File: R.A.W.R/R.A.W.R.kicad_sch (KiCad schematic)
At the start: 15 parts, among them IC1 PSA4-5043+, J1 BNC connector

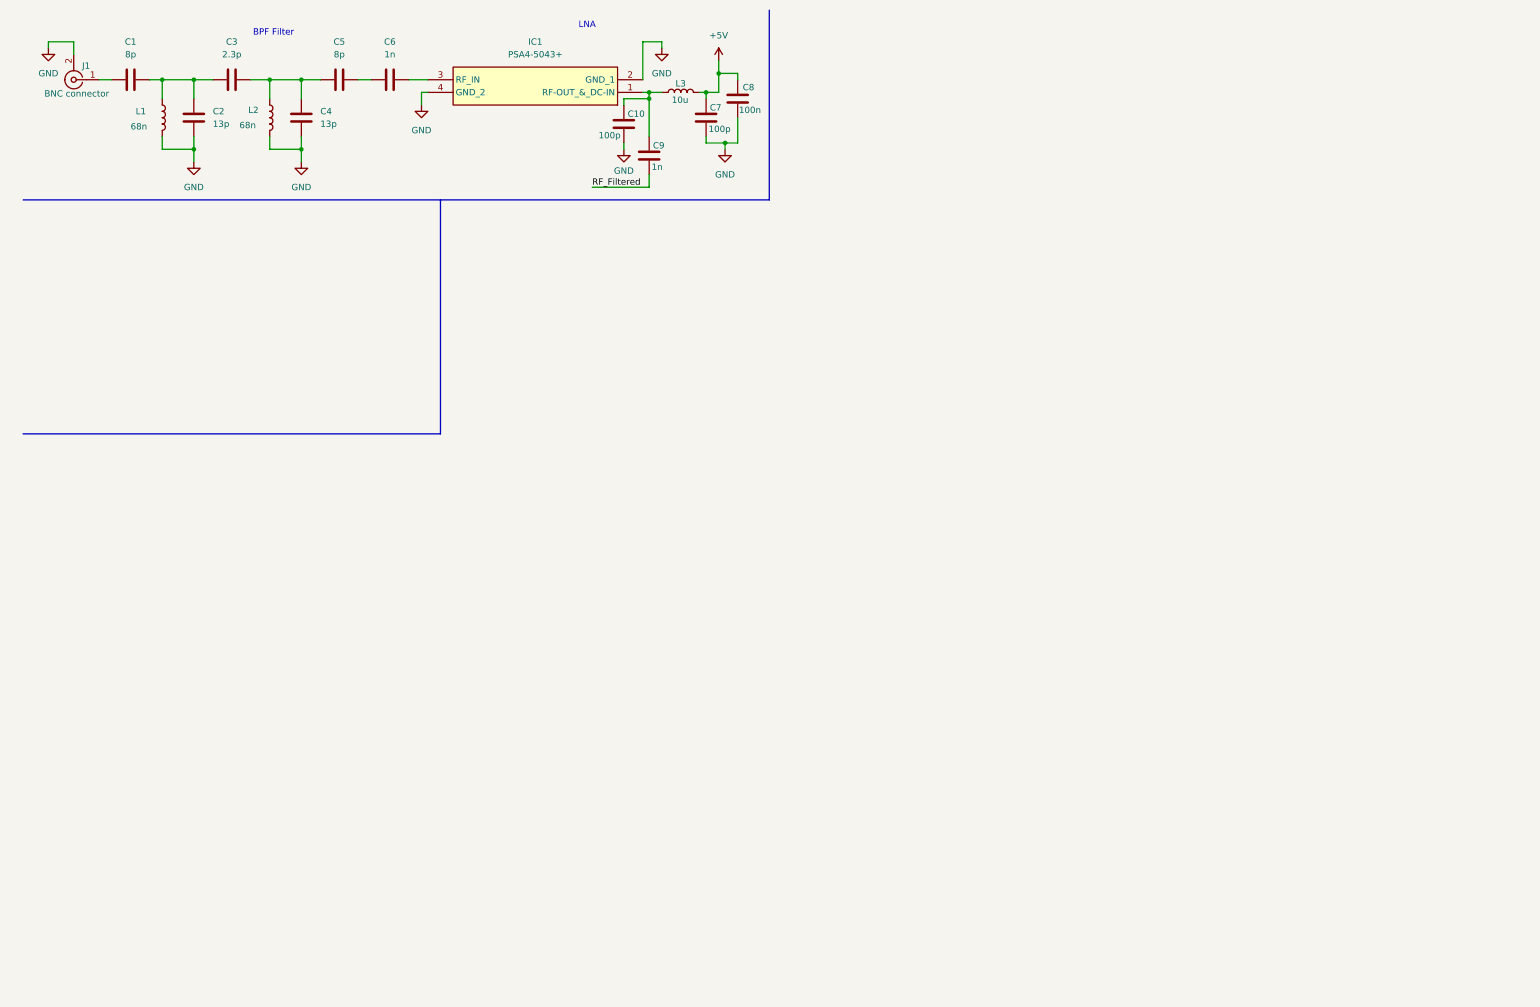
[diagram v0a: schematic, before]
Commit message: Added mixer, 10.7MHz filter, AM demodulator, audio amp and speaker
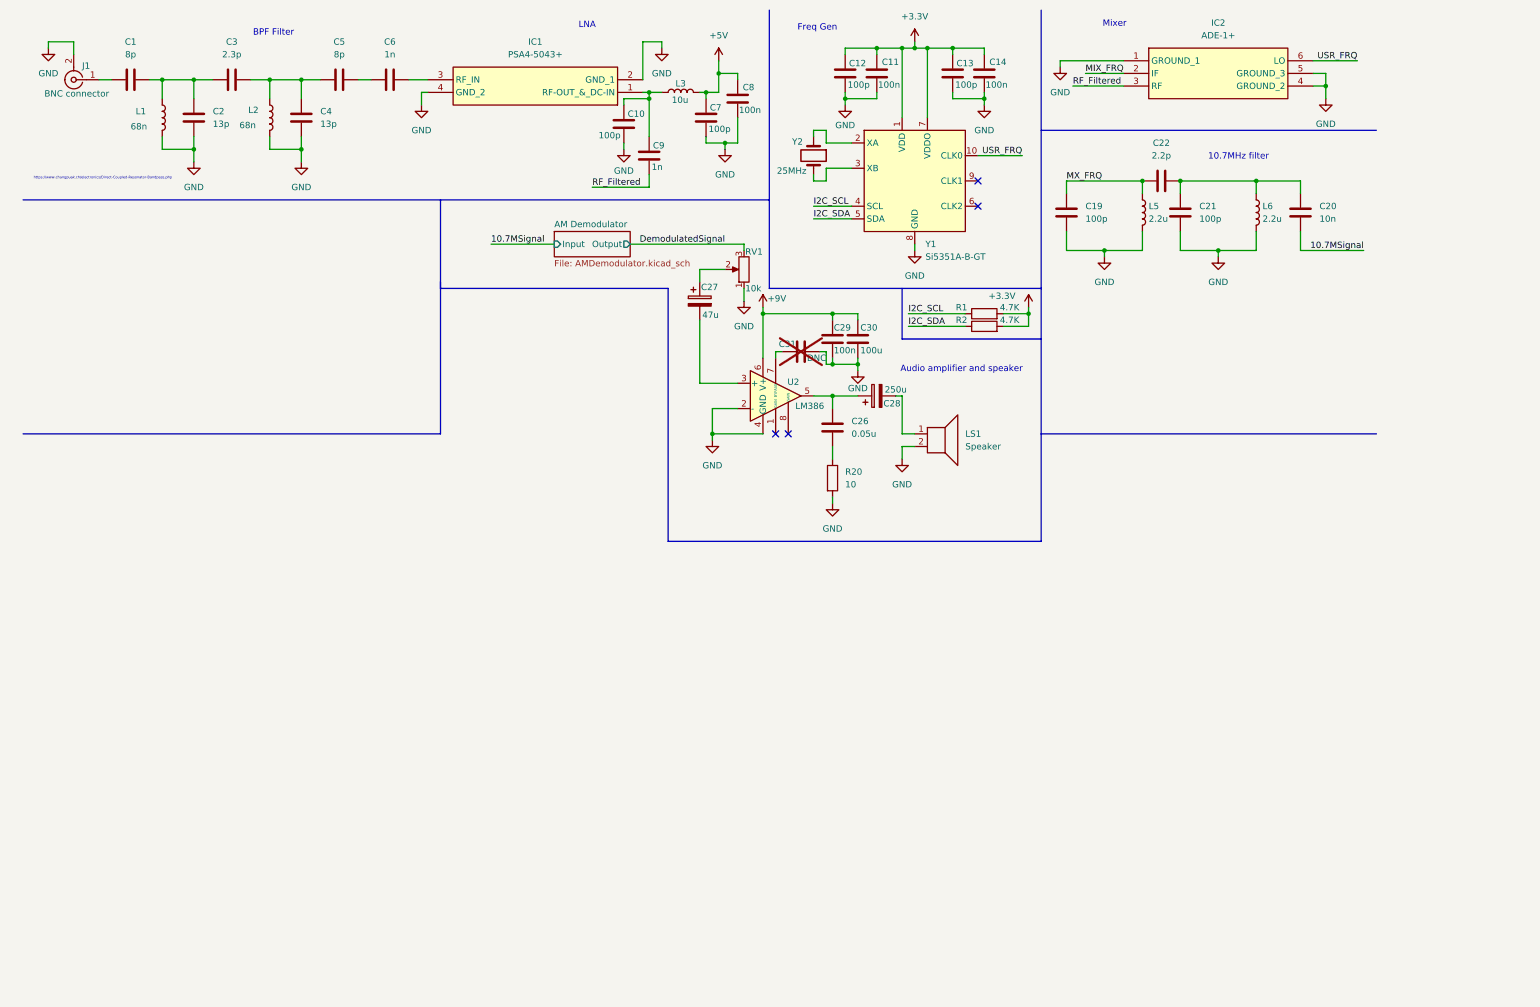
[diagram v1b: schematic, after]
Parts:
- added C11, C14, C29: 100n, symbol Device:C
- added C12, C13, C19, C21: 100p, symbol Device:C
- added C20: 10n, symbol Device:C
- added C22: 2.2p, symbol Device:C
- added C26: 0.05u, symbol Device:C
- added C27: 47u, symbol Device:C_Polarized
- added C28: 250u, symbol Device:C_Polarized
- added C30: 100u, symbol Device:C
- added C31: DNC, symbol Device:C
- added IC2: ADE-1+, ADE1, symbol RAWR:ADE-1+
- added L5, L6: 2.2u, Package_SO:SOIC-20W_7.5x12.8mm_P1.27mm, symbol Device:L
- added LS1: Speaker, Package_SON:WSON-8-1EP_6x5mm_P1.27mm_EP3.4x4mm, symbol Device:Speaker
- added R1, R2: 4.7K, symbol Device:R
- added R20: 10, symbol Device:R
- added RV1: 10k, Package_SO:TSSOP-20_4.4x6.5mm_P0.65mm, symbol Device:R_Potentiometer
- added U2: LM386, Package_DIP:DIP-14_W7.62mm, symbol Amplifier_Audio:LM386
- added Y1: Si5351A-B-GT, Package_SO:MSOP-10_3x3mm_P0.5mm, symbol Oscillator:Si5351A-B-GT
- added Y2: 25MHz, symbol Device:Crystal
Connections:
- net GND: now also C11.1, C12.1, C13.1, C14.1, C19.2, C21.2, C29.2, C30.2, C31.2, IC2.1 (GROUND_1), IC2.4 (GROUND_2), IC2.5 (GROUND_3), L5.2, L6.2, LS1.2, R20.2, RV1.1, U2.2 (-), U2.4 (GND), Y1.8 (GND)
- net RF_Filtered: now also IC2.3 (RF)
- new net: C27.1, RV1.2
- new net: C27.2, U2.3 (+)
- new net: C26.2, R20.1
- new net: C20.1, C21.1, C22.2, L6.1
- new net: C26.1, C28.1, U2.5
- new net: C28.2, LS1.1
- new net: Y1.2 (XA), Y2.1
- new net: Y1.3 (XB), Y2.2
- new net: C31.1, U2.7 (BYPASS)
- new net +3.3V: C11.2, C12.2, C13.2, C14.2, R1.2, R2.2, Y1.1 (VDD), Y1.7 (VDDO)
- new net +9V: C29.1, C30.1, U2.6 (V+)
- new net 10.7MSignal: C20.2
- new net DemodulatedSignal: RV1.3
- new net I2C_SCL: R1.1, Y1.4 (SCL)
- new net I2C_SDA: R2.1, Y1.5 (SDA)
- new net MIX_FRQ: IC2.2 (IF)
- new net MX_FRQ: C19.1, C22.1, L5.1
- new net USR_FRQ: IC2.6 (LO), Y1.10 (CLK0)
- no-connect marks 0 -> 4
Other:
- added sheet AM Demodulator (AMDemodulator.kicad_sch)
- note added: "10.7MHz filter"
- note added: "Audio amplifier and speaker"
- note added: "Freq Gen"
- note added: "Mixer"
- note added: "https://www.changpuak.ch/electronics/Direct-Coupled-Resonator-Bandpass.php"
- company: (none) -> Author: Wiktor Kociuba
- title: (none) -> R.A.W.R.

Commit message: Added RP2354A, screen and rotary encoder
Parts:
- added J3: 0.96 inch screen, Package_DFN_QFN:NXP_LQFN-48-1EP_7x7mm_P0.5mm_EP3.5x3.5mm_16xMask0.45x0.45_ThermalVias, symbol Connector:Conn_01x04_Pin
- added R27, R28, R29, R30, R31: 4.7K, symbol Device:R
- added SW3: RotaryEncoder_Switch, symbol Device:RotaryEncoder_Switch
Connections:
- net +3.3V: now also R27.2, R28.2
- net GND: now also J3.4 (Pin_4), SW3.C, SW3.S2
- new net +3V3: J3.3 (Pin_3), R29.2, R30.2, R31.2
- new net EncoderA: R29.1, SW3.A
- new net EncoderB: R30.1, SW3.B
- new net EncoderSW: R31.1, SW3.S1
- new net I2C1_SCL: J3.2 (Pin_2), R27.1
- new net I2C1_SDA: J3.1 (Pin_1), R28.1
- no-connect marks 4 -> 27
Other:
- added sheet MCU (MCU.kicad_sch)

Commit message: Added some footprints and USB-C receptacle
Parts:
- added C47, C48: 8p-30p, Capacitor_SMD:C_Trimmer_Murata_TZC3, symbol Device:C_Variable
- C1, C10, C11, C12, C13, C14, C2, C20, C22, C26, C29, C3, C31, C4, C5, C6, C7, C8, C9: footprint (none) -> Capacitor_SMD:C_0805_2012Metric_Pad1.18x1.45mm_HandSolder
- C19, C21: value 100p -> 82p; footprint (none) -> Capacitor_SMD:C_0805_2012Metric_Pad1.18x1.45mm_HandSolder
- C27, C28, C30: footprint (none) -> Capacitor_THT:CP_Radial_D8.0mm_P5.00mm
- IC1: footprint PSA45043 -> RAWR:PSA45043
- IC2: footprint ADE1 -> RAWR:ADE1
- J1: footprint Filter:Filter_Murata_BNX025 -> Connector_Coaxial:BNC_Amphenol_031-6575_Horizontal
- J3: footprint Package_DFN_QFN:NXP_LQFN-48-1EP_7x7mm_P0.5mm_EP3.5x3.5mm_16xMask0.45x0.45_ThermalVias -> Connector_PinHeader_2.54mm:PinHeader_1x04_P2.54mm_Vertical
- L1, L2, L3: footprint Package_SO:SOIC-20W_7.5x12.8mm_P1.27mm -> Inductor_SMD:L_0805_2012Metric_Pad1.05x1.20mm_HandSolder
- L5, L6: footprint Package_SO:SOIC-20W_7.5x12.8mm_P1.27mm -> Capacitor_SMD:C_0805_2012Metric_Pad1.18x1.45mm_HandSolder
- LS1: footprint Package_SON:WSON-8-1EP_6x5mm_P1.27mm_EP3.4x4mm -> Connector_PinHeader_2.54mm:PinHeader_1x02_P2.54mm_Vertical
- R1, R2, R20, R27, R28, R29, R30, R31: footprint (none) -> Resistor_SMD:R_0805_2012Metric_Pad1.20x1.40mm_HandSolder
- RV1: footprint Package_SO:TSSOP-20_4.4x6.5mm_P0.65mm -> (none)
- U2: footprint Package_DIP:DIP-14_W7.62mm -> (none)
- Y1: footprint Package_SO:MSOP-10_3x3mm_P0.5mm -> RAWR:SOP50P490X110-10N
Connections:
- net GND: now also C47.2, C48.2
- net MX_FRQ: now also C47.1
- net at C20.1, C21.1, C22.2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: now also C48.1

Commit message: Finished assignment of footprints
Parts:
- RV1: footprint (none) -> RAWR:PTV09A2020FA104
- SW3: footprint (none) -> RAWR:PEC11R4220FS0024
- U2: footprint (none) -> RAWR:SOIC127P600X175-8N
- Y2: footprint (none) -> Crystal:Crystal_SMD_5032-2Pin_5.0x3.2mm_HandSoldering
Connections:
- net MX_FRQ is gone; now on net MIX_FRQ: C19.1, C22.1, C47.1, L5.1
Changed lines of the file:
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@@
 		)
 	)
-	(label "MX_FRQ"
+	(label "MIX_FRQ"
 		(at 222.25 46.99 0)
 		(effects
@@
 			)
 		)
-		(property "Footprint" ""
+		(property "Footprint" "RAWR:PTV09A2020FA104"
 			(at 157.48 64.77 0)
 			(hide yes)
@@
 			)
 		)
-		(property "Footprint" ""
+		(property "Footprint" "Crystal:Crystal_SMD_5032-2Pin_5.0x3.2mm_HandSoldering"
 			(at 171.45 41.91 0)
 			(hide yes)
@@
 			)
 		)
-		(property "Footprint" ""
+		(property "Footprint" "RAWR:SOIC127P600X175-8N"
 			(at 166.37 87.63 0)
 			(hide yes)
@@
 			)
 		)
-		(property "Footprint" ""
+		(property "Footprint" "RAWR:PEC11R4220FS0024"
 			(at 45.72 126.746 0)
 			(hide yes)

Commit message: Added charger, 3v3 regulator and 10v5 stepup
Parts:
- added BT1: 18650 Li-Ion, Package_DFN_QFN:Texas_RGE0024H_VQFN-24-1EP_4x4mm_P0.5mm_EP2.7x2.7mm, symbol Device:Battery_Cell
- added C49, C51: 4.7u, QFN50P300X300X100-17N-D, symbol Device:C
- added C50, C66: 1u, QFN50P300X300X100-17N-D, symbol Device:C
- added C52: 100n, QFN50P300X300X100-17N-D, symbol Device:C
- added C53, C54, C58: 10u, QFN50P300X300X100-17N-D, symbol Device:C
- added C55, C56, C57, C63, C64, C65: 22u, QFN50P300X300X100-17N-D, symbol Device:C
- added C59, C67: 0.1u, QFN50P300X300X100-17N-D, symbol Device:C
- added C60: 2.2u, QFN50P300X300X100-17N-D, symbol Device:C
- added C61: 10n, QFN50P300X300X100-17N-D, symbol Device:C
- added C62: 100p, QFN50P300X300X100-17N-D, symbol Device:C
- added C68: 47n, QFN50P300X300X100-17N-D, symbol Device:C
- added D2: GREEN, symbol Device:LED
- added D3: RED, symbol Device:LED
- added IC3: BQ24075QRGTRQ1, QFN50P300X300X100-17N-D, symbol RAWR:BQ24075QRGTRQ1
- added IC4: TPS61088RHLR, RHL(R-PVQFN-N20)_1, symbol RAWR:TPS61088RHLR
- added L7, L8: 1.5u, SON50P300X400X100-15N-D, symbol Device:L
- added PS1: TPS63020DSJT, SON50P300X400X100-15N-D, symbol RAWR:TPS63020DSJT
- added R34, R35: 1.5k, symbol Device:R
- added R36: 1.18k, symbol Device:R
- added R37: 46.4k, symbol Device:R
- added R38: 1.13k, symbol Device:R
- added R39, R40, R41, R48: 10k, symbol Device:R
- added R42, R47, R49, R51: 100k, symbol Device:R
- added R43, R45: 1M, symbol Device:R
- added R44: 180k, symbol Device:R
- added R46: 255k, symbol Device:R
- added R50: 768k, symbol Device:R
- added SW4: SW_SPST, symbol Switch:SW_SPST
- added TH1: 10k, symbol Device:Thermistor
- IC1: footprint RAWR:PSA45043 -> PSA45043
- IC2: footprint RAWR:ADE1 -> ADE1
- Y1: footprint RAWR:SOP50P490X110-10N -> Package_SO:MSOP-10_3x3mm_P0.5mm
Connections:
- net +3V3: now also C55.1, C56.1, C57.1, PS1.4 (VOUT_1), PS1.5 (VOUT_2), R43.1, R45.2
- net GND: now also BT1.2 (-), C49.2, C50.2, C51.2, C52.2, C53.2, C54.2, C55.2, C56.2, C57.2, C58.2, C60.2, C61.2, C62.2, C63.2, C64.2, C65.2, C66.2, C67.2, C68.2, IC3.17 (EP), IC3.8 (VSS), IC4.11 (NC_1), IC4.12 (NC_2), IC4.13 (MODE), IC4.20 (AGND), IC4.21 (PGND), PS1.15 (EP), PS1.2 (GND), R36.2, R37.2, R38.2, R39.2, R40.2, R41.1, R44.1, R47.2, R49.2, R51.2, SW4.2 (B), TH1.2
- new net: D2.2 (A), R34.2
- new net: IC4.17 (FB), R49.1, R50.1
- new net: IC4.19 (ILIM), R47.1
- new net: C59.2, IC4.4 (SW_1), IC4.5 (SW_2), IC4.6 (SW_3), IC4.7 (SW_4), L8.1, R46.2
- new net: D3.1 (K), IC3.9 (~{CHG})
- new net: D3.2 (A), R35.1
- new net: C61.1, C62.1, R48.2
- new net: C59.1, IC4.8 (BOOT)
- new net: PS1.3 (FB), R43.2, R44.2
- new net: C60.1, IC4.1 (VCC)
- new net: C68.1, IC4.10 (SS)
- new net: IC4.18 (COMP), R48.1
- new net: IC4.3 (FSW), R46.1
- new net: IC3.1 (TS), TH1.1
- new net: C52.1, PS1.1 (VINA), PS1.12 (EN), PS1.13 (PS/SYNC)
- new net: L7.1, PS1.6 (L2_1), PS1.7 (L2_2)
- new net: L7.2, PS1.8 (L1_1), PS1.9 (L1_2)
- new net: IC3.16 (ISET), R38.1
- new net: IC3.14 (TMR), R37.1
- new net: IC3.12 (ILIM), R36.1
- new net: D2.1 (K), IC3.7 (~{PGOOD})
- new net +10V5: C63.1, C64.1, C65.1, C66.1, IC4.14 (VOUT_1), IC4.15 (VOUT_2), R50.2
- new net +BATT: BT1.1 (+), C49.1, IC3.2 (BAT_1), IC3.3 (BAT_2), R42.1
- new net EN1: IC3.6 (EN1), R39.1
- new net EN2: IC3.5 (EN2), R40.1
- new net EN_10V5: IC4.2 (EN), R51.1
- new net PG: PS1.14 (PG), R45.1
- new net SYSOFF: IC3.15 (SYSOFF), R42.2, SW4.1 (A)
- new net VBUS: C50.1, IC3.13 (IN)
- new net VSYS: C51.1, C53.1, C54.1, C58.1, C67.1, IC3.10 (OUT_1), IC3.11 (OUT_2), IC4.9 (VIN), L8.2, PS1.10 (VIN_1), PS1.11 (VIN_2), R34.1, R35.2
- new net ~{CE}: IC3.4 (~{CE}), R41.2
- no-connect marks 27 -> 22
